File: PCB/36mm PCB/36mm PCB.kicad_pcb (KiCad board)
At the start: 2 copper layers, 29.3 x 14.5 mm, 57 parts, among them IC1 PCF2003DUS, IC2 BMM350, IC3 STM32L011E4Y6TR, IC4 TPS22991BRAAR, IC5 MCP73831-2ACI_MC, Q3 2N7002KQBZ, Q4 2N7002KQBZ, Q5 2N7002KQBZ, Q6 2N7002KQBZ, SW5 SW_MEC_5E, U1 BMP581, Y1 ABS04W-32.768KHZ-4-D2-T5

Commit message: PCB 2.0
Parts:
- removed C1, C13, C4, C5: 100n, Capacitor_SMD:C_0201_0603Metric
- removed C12: 220n, Capacitor_SMD:C_0201_0603Metric
- removed C14: 4.7u, Capacitor_SMD:C_0201_0603Metric
- removed C2, C3, C6, C7: 1u, Capacitor_SMD:C_0201_0603Metric
- removed C8: 200n, Capacitor_SMD:C_0201_0603Metric
- removed D1, D2: D, Diode_SMD:D_0201_0603Metric
- removed IC3: STM32L011E4Y6TR, SamacSys_Parts:BGA25C40P5X5_213X207X58
- removed IC4: TPS22991BRAAR, SamacSys_Parts:TPS22991BRAAR
- removed L1: 27n, Inductor_SMD:L_0201_0603Metric
- removed R10: 100k, Resistor_SMD:R_0201_0603Metric
- removed TP1: GND_PCF2003, TestPoint:TestPoint_Pad_D1.0mm
- removed TP14: B+, TestPoint:TestPoint_Pad_D1.0mm
- removed TP15: B-, TestPoint:TestPoint_Pad_D1.0mm
- removed TP2: VDD_PCF2003, TestPoint:TestPoint_Pad_D1.0mm
- removed TP5: SWDIO, TestPoint:TestPoint_Pad_D1.0mm
- removed TP6: SWCLK, TestPoint:TestPoint_Pad_D1.0mm
- removed TP7: NRST, TestPoint:TestPoint_Pad_D1.0mm
- removed TPS3424-1: ~, Package_TO_SOT_SMD:SOT-583-8
- added C17: 100n, Capacitor_SMD:C_0201_0603Metric, F.Cu at (211.3, 118.3)
- added C18: 2.2u, Capacitor_SMD:C_0402_1005Metric, F.Cu at (207.6, 123.8)
- added C20: 220n, Capacitor_SMD:C_0201_0603Metric, F.Cu at (187.6, 118.5)
- added C21: 100n, Capacitor_SMD:C_0201_0603Metric, F.Cu at (189.9, 118.8)
- added C22: 4.7u, Capacitor_SMD:C_0402_1005Metric, F.Cu at (193.9, 123.7)
- added C23: 1u, Capacitor_SMD:C_0402_1005Metric, B.Cu at (196.7, 125.1)
- added C24: 100n, Capacitor_SMD:C_0201_0603Metric, B.Cu at (197.7, 125.0)
- added C25: 1u, Capacitor_SMD:C_0402_1005Metric, B.Cu at (194.7, 117.7)
- added C26: 1u, Capacitor_SMD:C_0402_1005Metric, F.Cu at (206.1, 121.2)
- added C27: 100n, Capacitor_SMD:C_0201_0603Metric, B.Cu at (204.1, 124.7)
- added C28: 100n, Capacitor_SMD:C_0201_0603Metric, B.Cu at (201.0, 126.9)
- added C29: 100n, Capacitor_SMD:C_0201_0603Metric, B.Cu at (202.9, 124.4)
- added C30: 1u, Capacitor_SMD:C_0402_1005Metric, B.Cu at (202.7, 125.3)
- added J1: Conn_01x04_Pin, SamacSys_Parts:Hall effect, F.Cu at (209.8, 116.4)
- added J2: Conn_01x02_Socket, SamacSys_Parts:Battery 36mm watch, F.Cu at (190.4, 115.1)
- added J3: Conn_01x02, SamacSys_Parts:Battery pogo pins, F.Cu at (193.3, 121.6)
- added LDLN025PU1: ~, Package_DFN_QFN:OnSemi_XDFN4-1EP_1.0x1.0mm_EP0.52x0.52mm, F.Cu at (193.8, 117.3)
- added LED1: 150060WS75000, SamacSys_Parts:150060WS75000, B.Cu at (192.9, 121.5)
- added Q7: 2N7002KQBZ, SamacSys_Parts:2N7002KQBZ, F.Cu at (197.2, 120.4)
- added R11: 10, Resistor_SMD:R_0402_1005Metric, B.Cu at (195.8, 117.7)
- added R19: 100k, Resistor_SMD:R_0201_0603Metric, B.Cu at (204.0, 126.2)
- added R20: 100k, Resistor_SMD:R_0201_0603Metric, B.Cu at (202.5, 126.2)
- added R22: 4.7k, Resistor_SMD:R_0201_0603Metric, B.Cu at (207.2, 118.1)
- added R23: 4.7k, Resistor_SMD:R_0201_0603Metric, B.Cu at (208.2, 118.1)
- added R7: 100k, Resistor_SMD:R_0201_0603Metric, F.Cu at (207.7, 121.0)
- added R8: 100k, Resistor_SMD:R_0201_0603Metric, F.Cu at (209.7, 119.7)
- added R9: 4.7k, Resistor_SMD:R_0201_0603Metric, B.Cu at (193.4, 120.1)
- added TP16: VDD Prog, SamacSys_Parts:Pogo pin 1x1, B.Cu at (204.4, 120.7)
- added TP19: NRST, SamacSys_Parts:Pogo pin 1x1, B.Cu at (204.1, 123.4)
- added TP20: 3.3V, SamacSys_Parts:Pogo pin 1x1, B.Cu at (195.7, 124.6)
- added TP21: VSS, SamacSys_Parts:Pogo pin 1x1, B.Cu at (197.5, 126.7)
- added TPS3424A11C13ADRLR1: ~, Package_TO_SOT_SMD:SOT-583-8, F.Cu at (191.5, 117.7)
- added U2: STM32L011F4Ux, Package_DFN_QFN:ST_UFQFPN-20_3x3mm_P0.5mm, B.Cu at (200.0, 124.7)
- C10, L2, L3, SW5, U1: moved to B.Cu
- C15: footprint Capacitor_SMD:C_0201_0603Metric -> Capacitor_SMD:C_0402_1005Metric
- CLPT1: value 1u -> 11.8n; footprint Capacitor_SMD:C_0201_0603Metric -> Capacitor_SMD:C_0402_1005Metric
- CSPT1: value 1u -> 4.7n; footprint Capacitor_SMD:C_0201_0603Metric -> Capacitor_SMD:C_0402_1005Metric
- R15: value 100k -> 47k
- R16: value 100k -> 1k
- R17: value 1k -> 2k
- R18: value 47k -> 100k
- R3: value 0 -> 4.7k
- R4: value 2k -> 4.7k
- R5: value 2k -> 4.7k; moved to B.Cu
- R6: value 2k -> 500; moved to B.Cu
- TP17: value Charge+ -> SWDIO; footprint TestPoint:TestPoint_Pad_D1.0mm -> SamacSys_Parts:Pogo pin 1x1; moved to B.Cu
- TP18: value Charge- -> SWCLK; footprint TestPoint:TestPoint_Pad_D1.0mm -> SamacSys_Parts:Pogo pin 1x1; moved to B.Cu
- Y1: value ABS04W-32.768KHZ-4-D2-T5 -> LFXTAL062558Reel; footprint SamacSys_Parts:ABS04W32768KHZ4D2T5 -> SamacSys_Parts:LFXTAL062558Reel
- moved R17 98.6 mm to (199.1, 121.0), turned to -65 degrees
- moved CLPT1 97.2 mm to (193.2, 119.5), turned to 115 degrees
- moved R18 95.2 mm to (195.9, 121.1), turned to -65 degrees
- moved CSPT1 95.0 mm to (191.7, 120.2), turned to 115 degrees
- moved C11 93.7 mm to (206.7, 124.0), turned to 90 degrees
- moved C9 92.7 mm to (205.8, 122.2), turned to 180 degrees
- moved R4 89.1 mm to (203.9, 122.9), turned to -90 degrees
- moved IC2 88.1 mm to (205.4, 123.5), turned to 90 degrees
- moved Y1 86.1 mm to (207.1, 118.3), turned to 90 degrees
- moved TP18 85.5 mm to (199.5, 121.8), turned to 180 degrees
- moved C15 84.6 mm to (194.8, 125.5), turned to -65 degrees
- moved TP17 83.7 mm to (197.2, 122.8), turned to 180 degrees
- moved R3 83.2 mm to (203.9, 124.4), turned to 90 degrees
- moved IC5 82.3 mm to (196.8, 123.2), turned to 25 degrees
- moved U1 81.2 mm to (192.2, 118.2), turned to 180 degrees
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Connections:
- net Net-(IC1-VDD) renamed /Main dial/VDD PROG
- C10 pad 2: Net-(U1-VDDIO) -> /Peripherals/VDDIO
- C11 pad 2: Controller Output -> +3.3V
- C9 pad 1: Controller Output -> GND
- C9 pad 2: GND -> +3.3V
- IC1 pad B2: OSCIN -> /Main dial/OSCIN
- IC1 pad C1: OSCOUT -> /Main dial/OSCOUT
- IC2 pad A2: I2C1_SDA -> /I2C_SDA
- IC2 pad A3: I2C1_SCL -> /I2C_SCL
- IC2 pad B3: Controller Output -> +3.3V
- IC2 pad C1: Controller Output -> +3.3V
- IC5 pad 1: Net-(IC5-VDD_1) -> /Power/Charge +
- IC5 pad 2: Net-(IC5-VDD_1) -> /Power/Charge +
- IC5 pad 5: Stat -> /Power/STAT
- Q3 pad 1: Tim2_CH3 -> /H_Tim1
- Q3 pad 2: Controller Output -> +3.3V
- Q4 pad 1: Tim2_CH1 -> /H_Tim2
- Q4 pad 2: Controller Output -> +3.3V
- Q5 pad 1: Tim2_CH1 -> /H_Tim2
- Q6 pad 1: Tim2_CH3 -> /H_Tim1
- R13 pad 1: Controller Output -> Net-(Q4-D_1)
- R13 pad 2: Tim2_CH3 -> /H_Tim1
- R14 pad 1: Tim2_CH1 -> +3.3V
- R14 pad 2: Controller Output -> /H_Tim2
- R15 pad 1: Tim2_CH1 -> Net-(C20-Pad2)
- R15 pad 2: Net-(Q3-D_1) -> /Button press
- R16 pad 1: Net-(Q4-D_1) -> Net-(C20-Pad2)
- R16 pad 2: Tim2_CH3 -> GND
- R17 pad 1: GND -> Net-(Q7-D_1)
- R17 pad 2: Net-(C12-Pad2) -> Net-(IC5-PROG)
- R18 pad 1: Net-(C12-Pad2) -> /Power/Charge +
- R18 pad 2: GPIO_EXTI9 -> GND
- R3 pad 1: Net-(IC1-RESET) -> +3.3V
- R3 pad 2: +3V0 -> /I2C_SDA
- R4 pad 1: Controller Output -> +3.3V
- R4 pad 2: I2C1_SDA -> /I2C_SCL
- R5 pad 1: Controller Output -> /I2C_SCL
- R5 pad 2: I2C1_SCL -> +3.3V
- R6 pad 1: Net-(IC5-PROG) -> /Power/STAT
- R6 pad 2: GND -> Net-(LED1-K)
- SW5 pad 1: Net-(C12-Pad2) -> Net-(C20-Pad2)
- SW5 pad 2: Net-(C12-Pad2) -> +3V0
- SW5 pad 3: +3V0 -> Net-(C20-Pad2)
- TP17 pad 1: Net-(IC5-VDD_1) -> /SWDIO
- TP18 pad 1: GND -> /SWCLK
- U1 pad 1: Net-(U1-VDDIO) -> /Peripherals/VDDIO
- U1 pad 10: Controller Output -> /Peripherals/VDDIO
- U1 pad 2: I2C1_SCL -> /I2C_SCL
- U1 pad 4: I2C1_SDA -> /I2C_SDA
- U1 pad 6: unconnected-(U1-CSB-Pad6) -> /Peripherals/VDDIO
- U1 pad 7: GND -> /BMP581_INT
- Y1 pad 1: OSCIN -> /Main dial/OSCOUT
- Y1 pad 2: GND -> /Main dial/OSCIN
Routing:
- net /I2C_SDA: track 0.00 -> 34.0 mm, vias 0 -> 4
- net /I2C_SCL: track 0.00 -> 32.7 mm, vias 0 -> 4
- net /H_Tim1: track 0.00 -> 24.4 mm, vias 0 -> 2
- net +3.3V: track 0.00 -> 23.2 mm, vias 0 -> 14
- net /H_Tim2: track 0.00 -> 18.9 mm, vias 0 -> 2
- net /KeepOn: track 0.00 -> 17.4 mm, vias 0 -> 1
- net /Button press: track 0.00 -> 16.3 mm, vias 0 -> 1
- net /Kill: track 0.00 -> 14.9 mm, vias 0 -> 1
- net /BMP581_INT: track 0.00 -> 13.6 mm
- net /L-S press INT: track 0.00 -> 13.4 mm, vias 0 -> 1
- net /Main dial/VDD PROG: track 0.00 -> 6.17 mm, vias 0 -> 1
- net Net-(Q4-D_1): track 0.00 -> 6.02 mm, vias 0 -> 1
- net Net-(IC1-RESET): track 0.00 -> 5.47 mm
- net /Power/STAT: track 0.00 -> 5.06 mm, vias 0 -> 1
- net +3V0: track 0.00 -> 4.93 mm, vias 0 -> 8
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- added copper zone on F.Cu, net +3.3V
- added copper zone on In3.Cu, net +3.3V
- added copper zone on F.Cu, net +3V0
- added copper zone on In2.Cu, net +3V0
- added copper zone on F.Cu, net /Power/Charge +
- added copper zone on B.Cu, net GND
- added copper zone on F.Cu, net GND
- added copper zone on In1.Cu, net GND
- added copper zone on In4.Cu, net GND
- added copper zone on F.Cu, net Net-(C20-Pad2)
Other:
- board size 29.3 x 14.5 mm -> 29.1 x 14.4 mm
- copper layers 2 -> 6

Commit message: Safety push
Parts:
- moved J2 0.18 mm to (190.5, 115.3)
- moved C21 0.09 mm to (189.9, 118.7)
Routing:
- net +3.3V: track 23.2 -> 25.6 mm, vias 14 -> 15
- net GND: track 0.00 -> 1.33 mm, vias 17 -> 46
- net /Peripherals/VDDIO: track 4.57 -> 5.62 mm
- net Net-(C20-Pad2): vias 0 -> 2

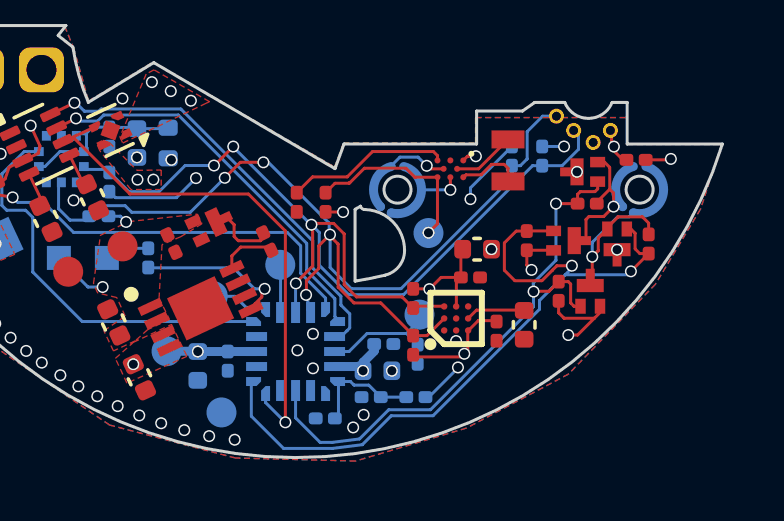
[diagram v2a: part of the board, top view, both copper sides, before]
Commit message: STM32 BLE + H chip
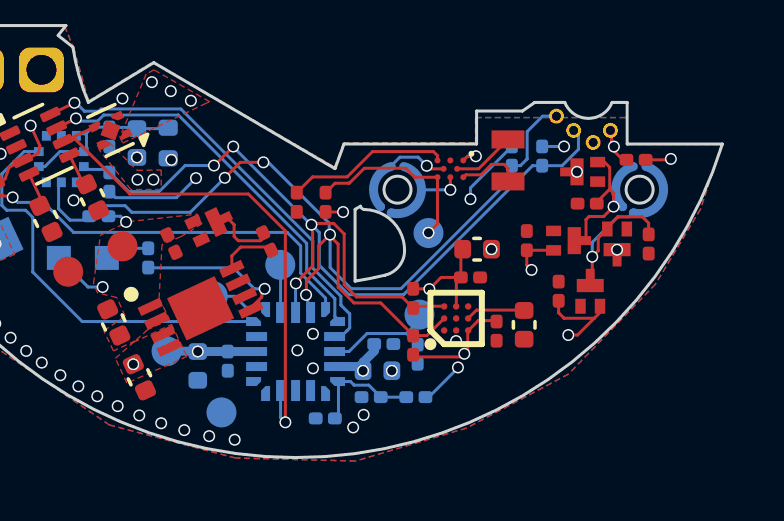
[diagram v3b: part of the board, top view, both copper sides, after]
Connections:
- R16 pad 1: Net-(C20-Pad2) -> +3V0
- R16 pad 2: GND -> Net-(C20-Pad2)
- SW5 pad 1: Net-(C20-Pad2) -> GND
- SW5 pad 2: +3V0 -> Net-(C20-Pad2)
- SW5 pad 3: Net-(C20-Pad2) -> GND
- SW5 pad 4: +3V0 -> Net-(C20-Pad2)
- U2 pad 10: /KeepOn -> unconnected-(U2-PA7-Pad10)
- U2 pad 11: /H_Tim1 -> unconnected-(U2-PB1-Pad11)
- U2 pad 6: unconnected-(U2-PA1-Pad6) -> /H_Tim1
- U2 pad 9: unconnected-(U2-PA6-Pad9) -> /KeepOn
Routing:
- net /H_Tim1: track 24.7 -> 0.00 mm, vias 2 -> 0
- net /H_Tim2: track 19.2 -> 0.00 mm, vias 2 -> 0
- net GND: vias 46 -> 48
- net +3V0: vias 8 -> 6
